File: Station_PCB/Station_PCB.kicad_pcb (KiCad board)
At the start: 2 copper layers, 91.4 x 73.7 mm, 13 parts, among them J1 Conn_01x19_Socket, J10 Conn_01x04_Socket, J11 Conn_01x06_Socket, J2 Conn_01x19_Socket, J3 Conn_01x08_Socket, J4 Conn_01x08_Socket, J5 Conn_01x04_Socket, J6 Conn_01x19_Socket, J7 Conn_01x19_Socket, J8 Conn_01x08_Socket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

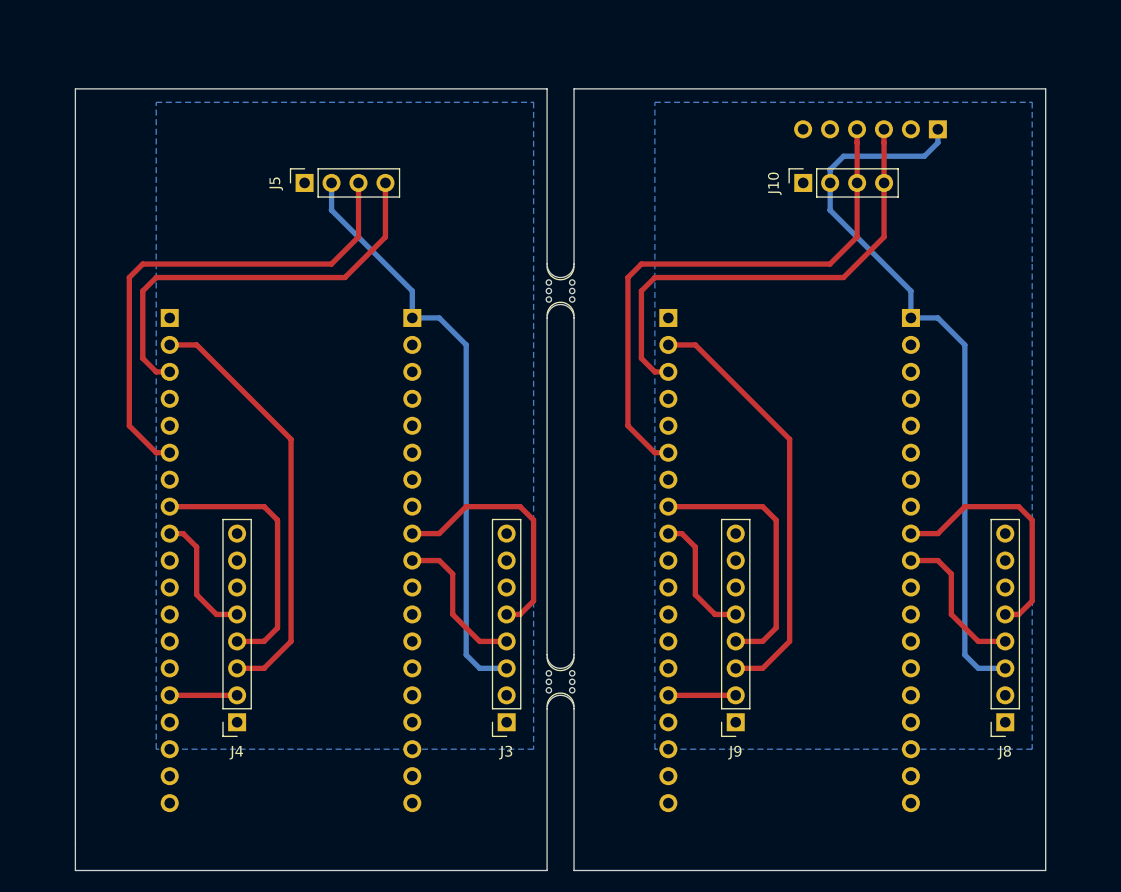
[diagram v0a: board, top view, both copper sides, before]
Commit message: Corregir parametros de pistas y agregar mounthing holes
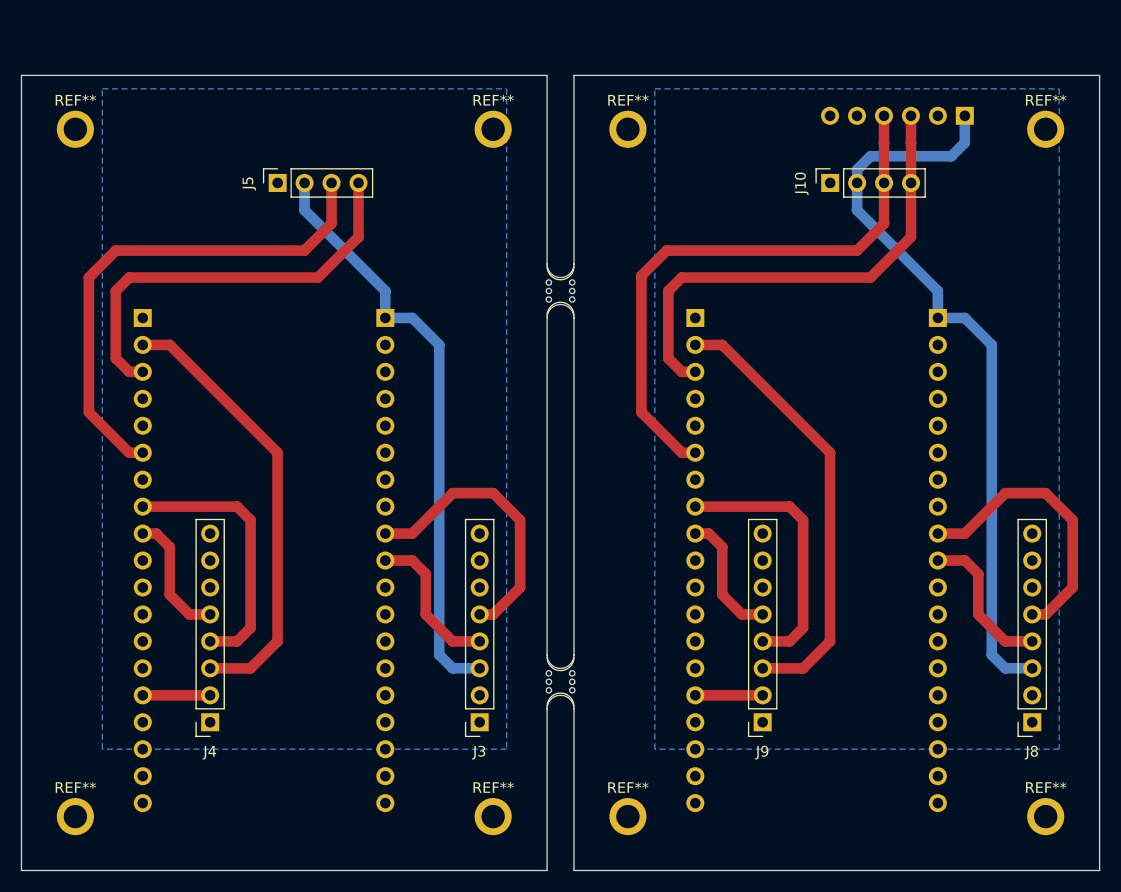
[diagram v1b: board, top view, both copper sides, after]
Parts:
- added REF**: MountingHole_2.2mm_M2_ISO7380_Pad, MountingHole:MountingHole_2.2mm_M2_ISO7380_Pad, F.Cu at (116.8, 58.4)
- added REF**: MountingHole_2.2mm_M2_ISO7380_Pad, MountingHole:MountingHole_2.2mm_M2_ISO7380_Pad, F.Cu at (129.5, 123.2)
- added REF**: MountingHole_2.2mm_M2_ISO7380_Pad, MountingHole:MountingHole_2.2mm_M2_ISO7380_Pad, F.Cu at (129.5, 58.4)
- added REF**: MountingHole_2.2mm_M2_ISO7380_Pad, MountingHole:MountingHole_2.2mm_M2_ISO7380_Pad, F.Cu at (116.8, 123.2)
- added REF**: MountingHole_2.2mm_M2_ISO7380_Pad, MountingHole:MountingHole_2.2mm_M2_ISO7380_Pad, F.Cu at (168.9, 123.2)
- added REF**: MountingHole_2.2mm_M2_ISO7380_Pad, MountingHole:MountingHole_2.2mm_M2_ISO7380_Pad, F.Cu at (77.5, 58.4)
- added REF**: MountingHole_2.2mm_M2_ISO7380_Pad, MountingHole:MountingHole_2.2mm_M2_ISO7380_Pad, F.Cu at (168.9, 58.4)
- added REF**: MountingHole_2.2mm_M2_ISO7380_Pad, MountingHole:MountingHole_2.2mm_M2_ISO7380_Pad, F.Cu at (77.5, 123.2)
- moved J11 2.84 mm to (161.3, 57.1)
- moved J9 2.54 mm to (142.2, 114.3)
- moved J2 2.54 mm to (83.8, 76.2)
- moved J3 2.54 mm to (115.6, 114.3)
- moved J1 2.54 mm to (106.7, 76.2)
- moved J10 2.54 mm to (148.6, 63.5)
- moved J4 2.54 mm to (90.2, 114.3)
- moved J5 2.54 mm to (96.5, 63.5)
- moved J6 2.54 mm to (158.8, 76.2)
- moved J7 2.54 mm to (135.9, 76.2)
- moved J8 2.54 mm to (167.6, 114.3)
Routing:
- net /TX_module/IRQ: track 23.7 -> 26.6 mm
- net /RX_module/IRQ: track 23.7 -> 26.6 mm
- net /TX_module/SDA: track 52.2 -> 54.6 mm
- net /TX_module/MOSI: track 40.3 -> 42.1 mm
- net /RX_module/MOSI: track 40.3 -> 42.1 mm
- net +3.3V2: track 69.3 -> 70.6 mm
- net /TX_module/SCL: track 44.5 -> 45.8 mm
- net /RX_module/SDA: track 47.1 -> 48.2 mm
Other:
- board size 91.4 x 73.7 mm -> 101.6 x 74.9 mm

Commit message: Mejora placa y la deja en una sola cara para impresion
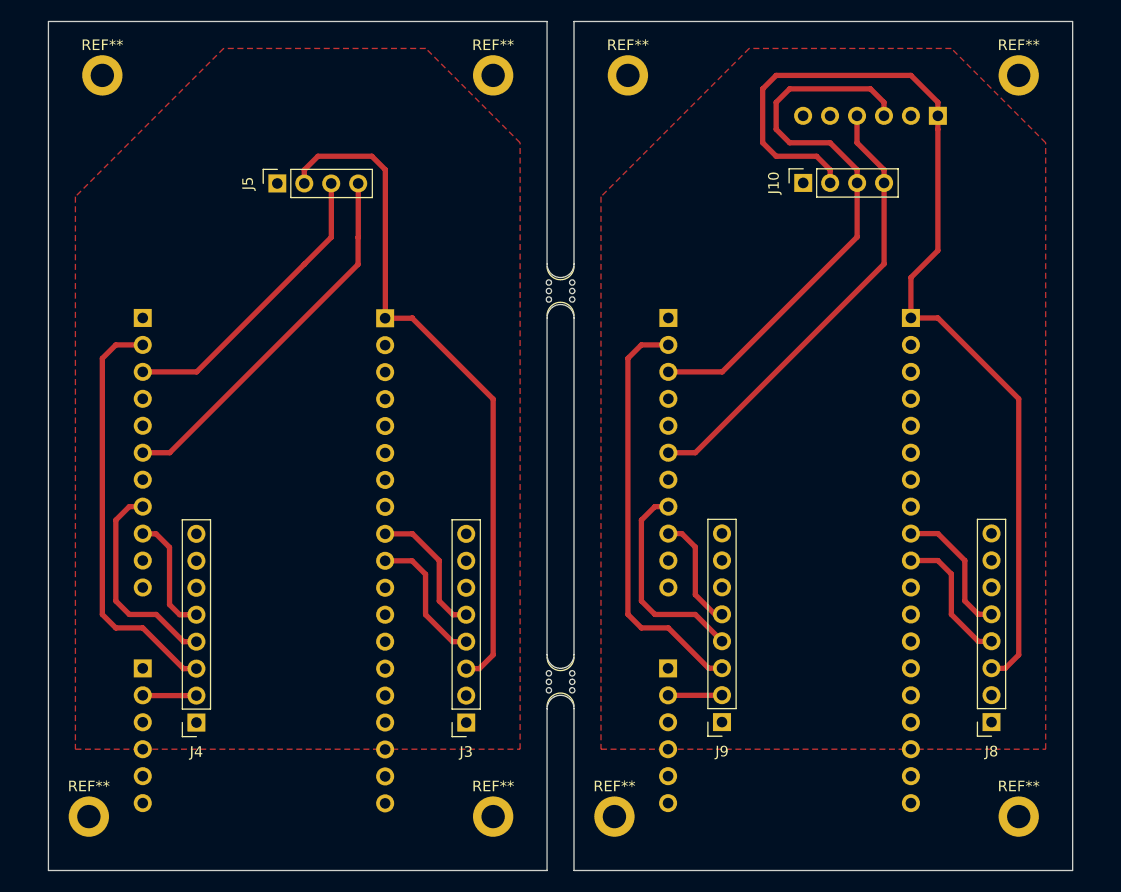
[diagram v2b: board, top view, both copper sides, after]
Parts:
- removed J2, J7: Conn_01x19_Socket, Connector_PinSocket_2.54mm:PinSocket_1x19_P2.54mm_Vertical
- removed the REF** at (116.8, 58.4)
- removed the REF** at (129.5, 123.2)
- removed the REF** at (129.5, 58.4)
- removed the REF** at (116.8, 123.2)
- removed the REF** at (168.9, 123.2)
- removed the REF** at (77.5, 58.4)
- removed the REF** at (168.9, 58.4)
- removed the REF** at (77.5, 123.2)
- added J2-1: Conn_01x11_Socket, Connector_PinSocket_2.54mm:PinSocket_1x11_P2.54mm_Vertical, B.Cu at (83.8, 76.2)
- added J2-2: Conn_01x06_Socket, Connector_PinSocket_2.54mm:PinSocket_1x06_P2.54mm_Vertical, B.Cu at (83.8, 109.2)
- added J7-1: Conn_01x11_Socket, Connector_PinSocket_2.54mm:PinSocket_1x11_P2.54mm_Vertical, B.Cu at (133.3, 76.2)
- added J7-2: Conn_01x06_Socket, Connector_PinSocket_2.54mm:PinSocket_1x06_P2.54mm_Vertical, B.Cu at (133.3, 109.2)
- added REF**: MountingHole_2.2mm_M2_ISO14580_Pad, MountingHole:MountingHole_2.2mm_M2_ISO14580_Pad, F.Cu at (166.4, 53.3)
- added REF**: MountingHole_2.2mm_M2_ISO14580_Pad, MountingHole:MountingHole_2.2mm_M2_ISO14580_Pad, F.Cu at (166.4, 123.2)
- added REF**: MountingHole_2.2mm_M2_ISO14580_Pad, MountingHole:MountingHole_2.2mm_M2_ISO14580_Pad, F.Cu at (116.8, 123.2)
- added REF**: MountingHole_2.2mm_M2_ISO14580_Pad, MountingHole:MountingHole_2.2mm_M2_ISO14580_Pad, F.Cu at (128.3, 123.2)
- added REF**: MountingHole_2.2mm_M2_ISO14580_Pad, MountingHole:MountingHole_2.2mm_M2_ISO14580_Pad, F.Cu at (116.8, 53.3)
- added REF**: MountingHole_2.2mm_M2_ISO14580_Pad, MountingHole:MountingHole_2.2mm_M2_ISO14580_Pad, F.Cu at (80.0, 53.3)
- added REF**: MountingHole_2.2mm_M2_ISO14580_Pad, MountingHole:MountingHole_2.2mm_M2_ISO14580_Pad, F.Cu at (129.5, 53.3)
- added REF**: MountingHole_2.2mm_M2_ISO14580_Pad, MountingHole:MountingHole_2.2mm_M2_ISO14580_Pad, F.Cu at (78.7, 123.2)
- moved J9 3.84 mm to (138.4, 114.3)
- moved J8 3.84 mm to (163.8, 114.3)
- moved J10 2.54 mm to (146.1, 63.5)
- moved J11 2.54 mm to (158.8, 57.1)
- moved J6 2.54 mm to (156.2, 76.2)
- moved J4 1.30 mm to (88.9, 114.3)
- moved J3 1.27 mm to (114.3, 114.3)
- moved J5 0.06 mm to (96.5, 63.5)
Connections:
- J10 pad 3: /TX_module/SDA -> /TX_module/SCL
- J10 pad 4: /TX_module/SCL -> /TX_module/SDA
- J5 pad 3: /RX_module/SDA -> /RX_module/SCL
- J5 pad 4: /RX_module/SCL -> /RX_module/SDA
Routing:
- net +3.3V2: track 70.6 -> 93.7 mm
- net /TX_module/IRQ: track 26.6 -> 13.0 mm
- net /RX_module/IRQ: track 26.6 -> 13.0 mm
- net /RX_module/SDA: track 48.2 -> 35.3 mm
- net /TX_module/SDA: track 54.6 -> 42.7 mm
- net /RX_module/SCL: track 39.5 -> 28.2 mm
- net +3.3V: track 55.6 -> 64.6 mm
- net /TX_module/SCL: track 45.8 -> 53.6 mm
- net /RX_module/MISO: track 25.2 -> 19.9 mm
- net /TX_module/MISO: track 25.2 -> 19.9 mm
- net /RX_module/MOSI: track 42.1 -> 39.4 mm
- net /TX_module/MOSI: track 42.1 -> 39.5 mm
- net /TX_module/SCK: track 11.7 -> 10.2 mm
- net /TX_module/RST: track 14.3 -> 13.0 mm
- net /TX_module/CS: track 6.33 -> 5.06 mm
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- added copper zone on F.Cu, net GND
- added copper zone on F.Cu, net GND2
- removed copper zone on B.Cu, net GND
- removed copper zone on B.Cu, net GND2
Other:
- board size 101.6 x 74.9 mm -> 96.5 x 80 mm

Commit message: Mover a cara trasera para impresion
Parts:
- removed the REF** at (166.4, 53.3)
- removed the REF** at (166.4, 123.2)
- removed the REF** at (116.8, 123.2)
- removed the REF** at (128.3, 123.2)
- removed the REF** at (116.8, 53.3)
- removed the REF** at (80.0, 53.3)
- removed the REF** at (129.5, 53.3)
- removed the REF** at (78.7, 123.2)
- added REF**: MountingHole_3mm_Pad, MountingHole:MountingHole_3mm_Pad, F.Cu at (77.5, 121.9)
- added REF**: MountingHole_3mm_Pad, MountingHole:MountingHole_3mm_Pad, F.Cu at (168.9, 121.9)
- added REF**: MountingHole_3mm_Pad, MountingHole:MountingHole_3mm_Pad, F.Cu at (129.5, 54.6)
- added REF**: MountingHole_3mm_Pad, MountingHole:MountingHole_3mm_Pad, F.Cu at (129.5, 121.9)
- added REF**: MountingHole_3mm_Pad, MountingHole:MountingHole_3mm_Pad, F.Cu at (116.8, 54.6)
- added REF**: MountingHole_3mm_Pad, MountingHole:MountingHole_3mm_Pad, F.Cu at (168.9, 54.6)
- added REF**: MountingHole_3mm_Pad, MountingHole:MountingHole_3mm_Pad, F.Cu at (116.8, 121.9)
- added REF**: MountingHole_3mm_Pad, MountingHole:MountingHole_3mm_Pad, F.Cu at (77.5, 54.6)
- moved J7-2 2.54 mm to (135.9, 109.2)
- moved J10 2.54 mm to (148.6, 63.5)
- moved J11 2.54 mm to (161.3, 57.1)
- moved J6 2.54 mm to (158.8, 76.2)
- moved J7-1 2.54 mm to (135.9, 76.2)
- moved J8 2.54 mm to (166.3, 114.3)
- moved J9 2.54 mm to (140.9, 114.3)
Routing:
- net /TX_module/SCK: track 10.2 -> 11.2 mm
- added copper zone on B.Cu, net GND
- added copper zone on B.Cu, net GND2
- removed copper zone on F.Cu, net GND
- removed copper zone on F.Cu, net GND2
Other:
- board size 96.5 x 80 mm -> 101.6 x 80 mm
